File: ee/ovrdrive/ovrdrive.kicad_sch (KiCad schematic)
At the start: 41 parts, among them J1 USB_A, J3 AVR-ISP-6, U1 SM3257ENT, U2 FLASH, U3 ATtiny24A-MM, U4 SN74LVC1G32DCKR, U5 DRV8837C

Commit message: R0.3 released
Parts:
- added C15, C16: 100nF, Capacitor_SMD:C_0603_1608Metric, symbol Device:C_Small
- R14, R15: footprint Resistor_SMD:R_0402_1005Metric -> Resistor_SMD:R_0603_1608Metric
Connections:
- net +3.3V: now also C15.1
- net +5V: now also C16.1
- net GND: now also C15.2, C16.2
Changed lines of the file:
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@@
   (junction (at 71.12 62.865) (diameter 0) (color 0 0 0 0)
   )
+  (junction (at 196.85 109.855) (diameter 0) (color 0 0 0 0)
+  )
   (junction (at 54.61 176.53) (diameter 0) (color 0 0 0 0)
   )
@@
   (junction (at 104.14 46.99) (diameter 0) (color 0 0 0 0)
   )
+  (junction (at 189.23 109.855) (diameter 0) (color 0 0 0 0)
+  )
   (junction (at 177.8 116.84) (diameter 0) (color 0 0 0 0)
   )
@@
     (stroke (width 0) (type default))
   )
+  (wire (pts (xy 189.23 109.855) (xy 189.23 110.49))
+    (stroke (width 0) (type default))
+  )
   (wire (pts (xy 104.775 89.535) (xy 99.06 89.535))
     (stroke (width 0) (type default))
@@
     (stroke (width 0) (type default))
   )
+  (wire (pts (xy 191.77 109.855) (xy 191.77 118.11))
+    (stroke (width 0) (type default))
+  )
   (wire (pts (xy 76.835 62.865) (xy 76.835 64.77))
     (stroke (width 0) (type default))
@@
     (stroke (width 0) (type default))
   )
+  (wire (pts (xy 196.85 109.855) (xy 196.85 110.49))
+    (stroke (width 0) (type default))
+  )
   (wire (pts (xy 37.465 59.055) (xy 43.18 59.055))
     (stroke (width 0) (type default))
@@
     (stroke (width 0) (type default))
   )
+  (wire (pts (xy 189.23 115.57) (xy 189.23 116.205))
+    (stroke (width 0) (type default))
+  )
   (wire (pts (xy 153.67 74.93) (xy 153.67 76.2))
     (stroke (width 0) (type default))
@@
     (stroke (width 0) (type default))
   )
-  (wire (pts (xy 191.77 109.855) (xy 191.77 118.11))
+  (wire (pts (xy 189.23 104.775) (xy 189.23 109.855))
     (stroke (width 0) (type default))
   )
@@
     (stroke (width 0) (type default))
   )
+  (wire (pts (xy 189.23 109.855) (xy 191.77 109.855))
+    (stroke (width 0) (type default))
+  )
   (wire (pts (xy 204.47 138.43) (xy 205.74 138.43))
     (stroke (width 0) (type default))
@@
     (stroke (width 0) (type default))
   )
-  (wire (pts (xy 194.31 114.935) (xy 194.31 118.11))
+  (wire (pts (xy 196.85 104.775) (xy 196.85 109.855))
     (stroke (width 0) (type default))
   )
@@
     (stroke (width 0) (type default))
   )
+  (wire (pts (xy 196.85 115.57) (xy 196.85 116.205))
+    (stroke (width 0) (type default))
+  )
   (wire (pts (xy 80.645 64.77) (xy 80.645 62.865))
     (stroke (width 0) (type default))
@@
     (stroke (width 0) (type default))
   )
+  (wire (pts (xy 194.31 109.855) (xy 194.31 118.11))
+    (stroke (width 0) (type default))
+  )
   (wire (pts (xy 170.18 87.63) (xy 173.355 87.63))
     (stroke (width 0) (type default))
@@
   )
   (wire (pts (xy 184.15 130.81) (xy 173.99 130.81))
+    (stroke (width 0) (type default))
+  )
+  (wire (pts (xy 196.85 109.855) (xy 194.31 109.855))
     (stroke (width 0) (type default))
   )
@@
         (path "/73c7e5ea-07c9-44ef-a9f8-630a9b8be271"
           (reference "#PWR036") (unit 1)
+        )
+      )
+    )
+  )
+  (symbol (lib_id "Device:C_Small") (at 196.85 113.03 0) (unit 1)
+    (in_bom yes) (on_board yes) (dnp no)
+    (property "Reference" "C15" (at 198.12 109.22 0)
+      (effects (font (size 1.27 1.27)) (justify left))
+    )
+    (property "Value" "100nF" (at 198.12 111.125 0)
+      (effects (font (size 1.27 1.27)) (justify left))
+    )
+    (property "Footprint" "Capacitor_SMD:C_0603_1608Metric" (at 196.85 113.03 0)
+      (effects (font (size 1.27 1.27)) hide)
+    )
+    (property "Datasheet" "~" (at 196.85 113.03 0)
+      (effects (font (size 1.27 1.27)) hide)
+    )
+    (property "MPN" "CC0603KRX7R7BB104" (at 196.85 113.03 0)
+      (effects (font (size 1.27 1.27)) hide)
+    )
+    (pin "1")
+    (pin "2")
+    (instances
+      (project "ovrdrive"
+        (path "/73c7e5ea-07c9-44ef-a9f8-630a9b8be271"
+          (reference "C15") (unit 1)
         )
       )
@@
       (effects (font (size 1.27 1.27)) (justify right))
     )
-    (property "Footprint" "Resistor_SMD:R_0402_1005Metric" (at 173.99 138.43 0)
+    (property "Footprint" "Resistor_SMD:R_0603_1608Metric" (at 173.99 138.43 0)
       (effects (font (size 1.27 1.27)) hide)
     )
@@
     )
   )
+  (symbol (lib_id "Device:C_Small") (at 189.23 113.03 0) (mirror y) (unit 1)
+    (in_bom yes) (on_board yes) (dnp no)
+    (property "Reference" "C16" (at 187.96 109.22 0)
+      (effects (font (size 1.27 1.27)) (justify left))
+    )
+    (property "Value" "100nF" (at 187.96 111.125 0)
+      (effects (font (size 1.27 1.27)) (justify left))
+    )
+    (property "Footprint" "Capacitor_SMD:C_0603_1608Metric" (at 189.23 113.03 0)
+      (effects (font (size 1.27 1.27)) hide)
+    )
+    (property "Datasheet" "~" (at 189.23 113.03 0)
+      (effects (font (size 1.27 1.27)) hide)
+    )
+    (property "MPN" "CC0603KRX7R7BB104" (at 189.23 113.03 0)
+      (effects (font (size 1.27 1.27)) hide)
+    )
+    (pin "1")
+    (pin "2")
+    (instances
+      (project "ovrdrive"
+        (path "/73c7e5ea-07c9-44ef-a9f8-630a9b8be271"
+          (reference "C16") (unit 1)
+        )
+      )
+    )
+  )
   (symbol (lib_id "power:GND") (at 20.32 76.2 0) (unit 1)
     (in_bom yes) (on_board yes) (dnp no)
@@
     )
   )
-  (symbol (lib_id "power:+5V") (at 191.77 109.855 0) (unit 1)
-    (in_bom yes) (on_board yes) (dnp no) (fields_autoplaced)
-    (property "Reference" "#PWR038" (at 191.77 113.665 0)
-      (effects (font (size 1.27 1.27)) hide)
-    )
-    (property "Value" "+5V" (at 191.77 106.2792 0)
-      (effects (font (size 1.27 1.27)))
-    )
-    (property "Footprint" "" (at 191.77 109.855 0)
-      (effects (font (size 1.27 1.27)) hide)
-    )
-    (property "Datasheet" "" (at 191.77 109.855 0)
+  (symbol (lib_id "power:+5V") (at 189.23 104.775 0) (unit 1)
+    (in_bom yes) (on_board yes) (dnp no) (fields_autoplaced)
+    (property "Reference" "#PWR038" (at 189.23 108.585 0)
+      (effects (font (size 1.27 1.27)) hide)
+    )
+    (property "Value" "+5V" (at 189.23 101.1992 0)
+      (effects (font (size 1.27 1.27)))
+    )
+    (property "Footprint" "" (at 189.23 104.775 0)
+      (effects (font (size 1.27 1.27)) hide)
+    )
+    (property "Datasheet" "" (at 189.23 104.775 0)
       (effects (font (size 1.27 1.27)) hide)
     )
@@
     )
   )
+  (symbol (lib_id "power:GND") (at 196.85 116.205 0) (unit 1)
+    (in_bom yes) (on_board yes) (dnp no) (fields_autoplaced)
+    (property "Reference" "#PWR07" (at 196.85 122.555 0)
+      (effects (font (size 1.27 1.27)) hide)
+    )
+    (property "Value" "GND" (at 196.85 120.6484 0)
+      (effects (font (size 1.27 1.27)) hide)
+    )
+    (property "Footprint" "" (at 196.85 116.205 0)
+      (effects (font (size 1.27 1.27)) hide)
+    )
+    (property "Datasheet" "" (at 196.85 116.205 0)
+      (effects (font (size 1.27 1.27)) hide)
+    )
+    (pin "1")
+    (instances
+      (project "ovrdrive"
+        (path "/73c7e5ea-07c9-44ef-a9f8-630a9b8be271"
+          (reference "#PWR07") (unit 1)
+        )
+      )
+    )
+  )
   (symbol (lib_id "Device:R_Small_US") (at 173.99 123.825 0) (mirror x) (unit 1)
     (in_bom yes) (on_board yes) (dnp no)
@@
       (effects (font (size 1.27 1.27)) (justify right))
     )
-    (property "Footprint" "Resistor_SMD:R_0402_1005Metric" (at 173.99 123.825 0)
+    (property "Footprint" "Resistor_SMD:R_0603_1608Metric" (at 173.99 123.825 0)
       (effects (font (size 1.27 1.27)) hide)
     )
@@
     )
   )
-  (symbol (lib_id "power:+3.3V") (at 194.31 114.935 0) (unit 1)
-    (in_bom yes) (on_board yes) (dnp no) (fields_autoplaced)
-    (property "Reference" "#PWR037" (at 194.31 118.745 0)
-      (effects (font (size 1.27 1.27)) hide)
-    )
-    (property "Value" "+3.3V" (at 194.31 111.3592 0)
-      (effects (font (size 1.27 1.27)))
-    )
-    (property "Footprint" "" (at 194.31 114.935 0)
-      (effects (font (size 1.27 1.27)) hide)
-    )
-    (property "Datasheet" "" (at 194.31 114.935 0)
+  (symbol (lib_id "power:+3.3V") (at 196.85 104.775 0) (unit 1)
+    (in_bom yes) (on_board yes) (dnp no)
+    (property "Reference" "#PWR037" (at 196.85 108.585 0)
+      (effects (font (size 1.27 1.27)) hide)
+    )
+    (property "Value" "+3.3V" (at 196.85 101.1992 0)
+      (effects (font (size 1.27 1.27)))
+    )
+    (property "Footprint" "" (at 196.85 104.775 0)
+      (effects (font (size 1.27 1.27)) hide)
+    )
+    (property "Datasheet" "" (at 196.85 104.775 0)
       (effects (font (size 1.27 1.27)) hide)
     )
@@
         )
       )
+    )
+  )
+  (symbol (lib_id "power:GND") (at 189.23 116.205 0) (mirror y) (unit 1)
+    (in_bom yes) (on_board yes) (dnp no) (fields_autoplaced)
+    (property "Reference" "#PWR011" (at 189.23 122.555 0)
+      (effects (font (size 1.27 1.27)) hide)
+    )
+    (property "Value" "GND" (at 189.23 120.6484 0)
+      (effects (font (size 1.27 1.27)) hide)
+    )
+    (property "Footprint" "" (at 189.23 116.205 0)
+      (effects (font (size 1.27 1.27)) hide)
+    )
+    (property "Datasheet" "" (at 189.23 116.205 0)
+      (effects (font (size 1.27 1.27)) hide)
+    )
+    (pin "1")
+    (instances
+      (project "ovrdrive"
+        (path "/73c7e5ea-07c9-44ef-a9f8-630a9b8be271"
+          (reference "#PWR011") (unit 1)
+        )
+      )

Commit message: Added BOM commmited leftover stuff.
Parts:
- R1, R2: MPN (none) -> RC0402FR-071ML
- U5: MPN (none) -> DRV8837CDSGR
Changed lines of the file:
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@@
       (effects (font (size 1.27 1.27)) hide)
     )
-    (property "MPN" "" (at 62.23 176.53 90)
+    (property "MPN" "RC0402FR-071ML" (at 62.23 176.53 90)
       (effects (font (size 1.27 1.27)) hide)
     )
@@
       (effects (font (size 1.27 1.27)) hide)
     )
-    (property "MPN" "" (at 33.655 176.53 90)
+    (property "MPN" "RC0402FR-071ML" (at 33.655 176.53 90)
       (effects (font (size 1.27 1.27)) hide)
     )
@@
       (effects (font (size 1.27 1.27)) hide)
     )
+    (property "MPN" "DRV8837CDSGR" (at 194.31 130.81 0)
+      (effects (font (size 1.27 1.27)) hide)
+    )

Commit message: Added license
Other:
- moved on the sheet: C15, C16, R14, R15, U5

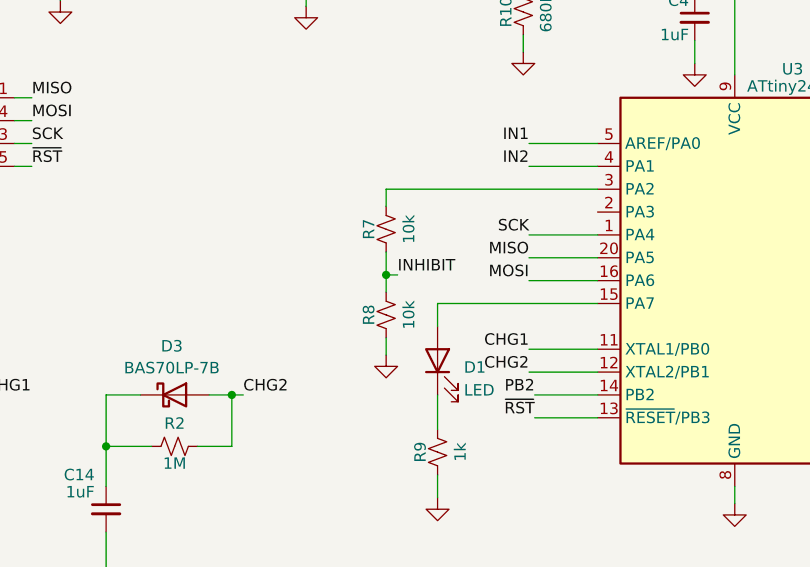
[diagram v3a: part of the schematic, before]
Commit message: Released R0.4 for *quote only*. Still need to do a final revision before sending off.
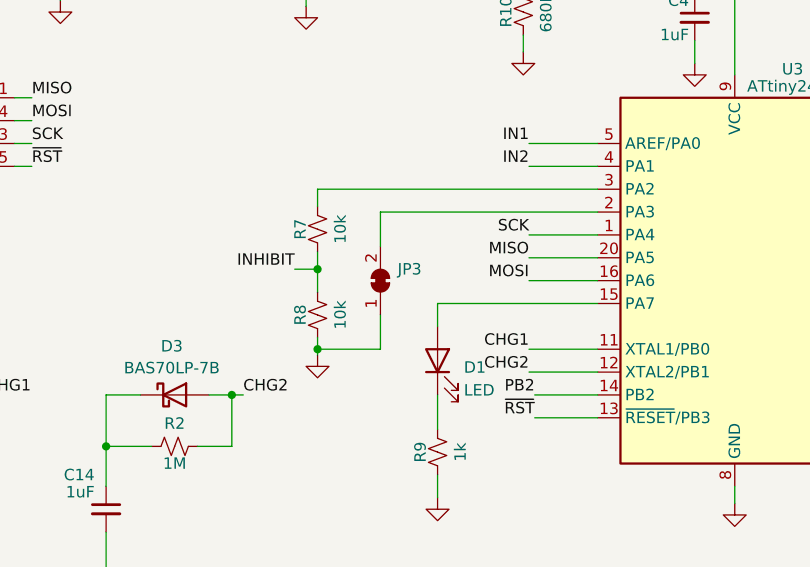
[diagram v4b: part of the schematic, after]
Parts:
- added JP3: SolderJumper_2_Bridged, Jumper:SolderJumper-2_P1.3mm_Bridged2Bar_RoundedPad1.0x1.5mm, symbol Jumper:SolderJumper_2_Bridged
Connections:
- net GND: now also JP3.1 (A)
- net at U3.2 (PA3): now also JP3.2 (B)
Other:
- moved on the sheet: R7, R8
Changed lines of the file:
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@@
   (junction (at 26.035 176.53) (diameter 0) (color 0 0 0 0)
   )
+  (junction (at 78.105 165.735) (diameter 0) (color 0 0 0 0)
+  )
   (junction (at 31.75 88.9) (diameter 0) (color 0 0 0 0)
   )
@@
   (junction (at 82.55 62.865) (diameter 0) (color 0 0 0 0)
   )
-  (junction (at 85.725 157.48) (diameter 0) (color 0 0 0 0)
-  )
   (junction (at 71.12 62.865) (diameter 0) (color 0 0 0 0)
   )
@@
   (junction (at 71.12 46.99) (diameter 0) (color 0 0 0 0)
   )
+  (junction (at 78.105 156.845) (diameter 0) (color 0 0 0 0)
+  )
   (junction (at 76.835 125.095) (diameter 0) (color 0 0 0 0)
   )
@@
     (stroke (width 0) (type default))
   )
+  (wire (pts (xy 85.09 165.735) (xy 78.105 165.735))
+    (stroke (width 0) (type default))
+  )
   (wire (pts (xy 54.61 111.125) (xy 46.99 111.125))
     (stroke (width 0) (type default))
@@
     (stroke (width 0) (type default))
   )
-  (wire (pts (xy 109.22 147.955) (xy 85.725 147.955))
-    (stroke (width 0) (type default))
-  )
   (wire (pts (xy 149.225 76.2) (xy 149.225 77.47))
     (stroke (width 0) (type default))
@@
     (stroke (width 0) (type default))
   )
+  (wire (pts (xy 85.09 150.495) (xy 109.22 150.495))
+    (stroke (width 0) (type default))
+  )
   (wire (pts (xy 120.015 131.445) (xy 120.015 133.985))
     (stroke (width 0) (type default))
@@
     (stroke (width 0) (type default))
   )
+  (wire (pts (xy 75.565 156.845) (xy 78.105 156.845))
+    (stroke (width 0) (type default))
+  )
   (wire (pts (xy 73.025 122.555) (xy 73.025 125.095))
     (stroke (width 0) (type default))
@@
     (stroke (width 0) (type default))
   )
-  (wire (pts (xy 85.725 157.48) (xy 86.995 157.48))
-    (stroke (width 0) (type default))
-  )
   (wire (pts (xy 139.7 95.25) (xy 99.06 95.25))
     (stroke (width 0) (type default))
@@
     (stroke (width 0) (type default))
   )
-  (wire (pts (xy 85.725 147.955) (xy 85.725 149.86))
+  (wire (pts (xy 78.105 147.955) (xy 78.105 149.86))
     (stroke (width 0) (type default))
   )
@@
     (stroke (width 0) (type default))
   )
+  (wire (pts (xy 78.105 165.735) (xy 78.105 166.37))
+    (stroke (width 0) (type default))
+  )
   (wire (pts (xy 149.225 69.85) (xy 149.225 68.58))
     (stroke (width 0) (type default))
@@
     (stroke (width 0) (type default))
   )
+  (wire (pts (xy 85.09 161.925) (xy 85.09 165.735))
+    (stroke (width 0) (type default))
+  )
   (wire (pts (xy 111.125 39.37) (xy 111.125 40.64))
     (stroke (width 0) (type default))
@@
     (stroke (width 0) (type default))
   )
+  (wire (pts (xy 78.105 156.845) (xy 78.105 159.385))
+    (stroke (width 0) (type default))
+  )
   (wire (pts (xy 143.51 68.58) (xy 149.225 68.58))
     (stroke (width 0) (type default))
@@
     (stroke (width 0) (type default))
   )
-  (wire (pts (xy 85.725 154.94) (xy 85.725 157.48))
-    (stroke (width 0) (type default))
-  )
   (wire (pts (xy 65.405 40.64) (xy 65.405 39.37))
     (stroke (width 0) (type default))
@@
     (stroke (width 0) (type default))
   )
+  (wire (pts (xy 85.09 150.495) (xy 85.09 154.305))
+    (stroke (width 0) (type default))
+  )
   (wire (pts (xy 156.21 114.3) (xy 156.21 116.84))
     (stroke (width 0) (type default))
@@
     (stroke (width 0) (type default))
   )
+  (wire (pts (xy 78.105 147.955) (xy 109.22 147.955))
+    (stroke (width 0) (type default))
+  )
   (wire (pts (xy 80.645 64.77) (xy 80.645 62.865))
     (stroke (width 0) (type default))
@@
     (stroke (width 0) (type default))
   )
-  (wire (pts (xy 85.725 157.48) (xy 85.725 159.385))
+  (wire (pts (xy 78.105 154.94) (xy 78.105 156.845))
     (stroke (width 0) (type default))
   )
@@
     (stroke (width 0) (type default))
   )
-  (wire (pts (xy 85.725 164.465) (xy 85.725 166.37))
+  (wire (pts (xy 78.105 164.465) (xy 78.105 165.735))
     (stroke (width 0) (type default))
   )
@@
     (effects (font (size 1.27 1.27)) (justify left bottom))
   )
-  (label "INHIBIT" (at 86.995 157.48 0) (fields_autoplaced)
-    (effects (font (size 1.27 1.27)) (justify left bottom))
+  (label "INHIBIT" (at 75.565 156.845 180) (fields_autoplaced)
+    (effects (font (size 1.27 1.27)) (justify right bottom))
   )
   (label "~{WP}" (at 52.07 106.045 180) (fields_autoplaced)
@@
     (effects (font (size 1 1)) (justify left bottom))
   )
-  (symbol (lib_id "power:GND") (at 85.725 166.37 0) (unit 1)
+  (symbol (lib_id "power:GND") (at 78.105 166.37 0) (unit 1)
     (in_bom yes) (on_board yes) (dnp no) (fields_autoplaced)
-    (property "Reference" "#PWR028" (at 85.725 172.72 0)
+    (property "Reference" "#PWR028" (at 78.105 172.72 0)
       (effects (font (size 1.27 1.27)) hide)
     )
-    (property "Value" "GND" (at 85.725 170.8134 0)
+    (property "Value" "GND" (at 78.105 170.8134 0)
       (effects (font (size 1.27 1.27)) hide)
     )
-    (property "Footprint" "" (at 85.725 166.37 0)
+    (property "Footprint" "" (at 78.105 166.37 0)
       (effects (font (size 1.27 1.27)) hide)
     )
-    (property "Datasheet" "" (at 85.725 166.37 0)
+    (property "Datasheet" "" (at 78.105 166.37 0)
       (effects (font (size 1.27 1.27)) hide)
     )
@@
     )
   )
-  (symbol (lib_id "Device:R_Small_US") (at 85.725 152.4 180) (unit 1)
+  (symbol (lib_id "Device:R_Small_US") (at 78.105 152.4 180) (unit 1)
     (in_bom yes) (on_board yes) (dnp no)
-    (property "Reference" "R7" (at 83.82 152.4 90)
+    (property "Reference" "R7" (at 76.2 152.4 90)
       (effects (font (size 1.27 1.27)))
     )
-    (property "Value" "10k" (at 88.265 152.4 90)
+    (property "Value" "10k" (at 80.645 152.4 90)
       (effects (font (size 1.27 1.27)))
     )
-    (property "Footprint" "Resistor_SMD:R_0402_1005Metric" (at 85.725 152.4 0)
+    (property "Footprint" "Resistor_SMD:R_0402_1005Metric" (at 78.105 152.4 0)
       (effects (font (size 1.27 1.27)) hide)
     )
-    (property "Datasheet" "~" (at 85.725 152.4 0)
+    (property "Datasheet" "~" (at 78.105 152.4 0)
       (effects (font (size 1.27 1.27)) hide)
     )
-    (property "MPN" "RC0402FR-0710KL" (at 85.725 152.4 90)
+    (property "MPN" "RC0402FR-0710KL" (at 78.105 152.4 90)
       (effects (font (size 1.27 1.27)) hide)
     )
@@
     )
   )
+  (symbol (lib_id "Jumper:SolderJumper_2_Bridged") (at 85.09 158.115 90) (unit 1)
+    (in_bom yes) (on_board yes) (dnp no) (fields_autoplaced)
+    (property "Reference" "JP3" (at 86.995 156.845 90)
+      (effects (font (size 1.27 1.27)) (justify right))
+    )
+    (property "Value" "SolderJumper_2_Bridged" (at 86.995 159.385 90)
+      (effects (font (size 1.27 1.27)) (justify right) hide)
+    )
+    (property "Footprint" "Jumper:SolderJumper-2_P1.3mm_Bridged2Bar_RoundedPad1.0x1.5mm" (at 85.09 158.115 0)
+      (effects (font (size 1.27 1.27)) hide)
+    )
+    (property "Datasheet" "~" (at 85.09 158.115 0)
+      (effects (font (size 1.27 1.27)) hide)
+    )
+    (pin "1")
+    (pin "2")
+    (instances
+      (project "ovrdrive"
+        (path "/73c7e5ea-07c9-44ef-a9f8-630a9b8be271"
+          (reference "JP3") (unit 1)
+        )
+      )
+    )
+  )
   (symbol (lib_id "Driver_Motor:DRV8837C") (at 224.79 138.43 0) (unit 1)
     (in_bom yes) (on_board yes) (dnp no)
@@
     )
   )
-  (symbol (lib_id "Device:R_Small_US") (at 85.725 161.925 180) (unit 1)
+  (symbol (lib_id "Device:R_Small_US") (at 78.105 161.925 180) (unit 1)
     (in_bom yes) (on_board yes) (dnp no)
-    (property "Reference" "R8" (at 83.82 161.925 90)
+    (property "Reference" "R8" (at 76.2 161.925 90)
       (effects (font (size 1.27 1.27)))
     )
-    (property "Value" "10k" (at 88.265 161.925 90)
+    (property "Value" "10k" (at 80.645 161.925 90)
       (effects (font (size 1.27 1.27)))
     )
-    (property "Footprint" "Resistor_SMD:R_0402_1005Metric" (at 85.725 161.925 0)
+    (property "Footprint" "Resistor_SMD:R_0402_1005Metric" (at 78.105 161.925 0)
       (effects (font (size 1.27 1.27)) hide)
     )
-    (property "Datasheet" "~" (at 85.725 161.925 0)
+    (property "Datasheet" "~" (at 78.105 161.925 0)
       (effects (font (size 1.27 1.27)) hide)
     )
-    (property "MPN" "RC0402FR-0710KL" (at 85.725 161.925 90)
+    (property "MPN" "RC0402FR-0710KL" (at 78.105 161.925 90)
       (effects (font (size 1.27 1.27)) hide)
     )

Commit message: Added new part numbers
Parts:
- JP3: now left out of the parts list
- U1: MPN SM3257ENT -> SM3257ENAA
- U2: MPN K9HDG08U1A -> MT29F64G08CBABAWP
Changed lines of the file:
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@@
       (effects (font (size 1.27 1.27)) hide)
     )
-    (property "MPN" "SM3257ENT" (at 76.835 93.345 0)
+    (property "MPN" "SM3257ENAA" (at 76.835 93.345 0)
       (effects (font (size 1.27 1.27)) hide)
     )
@@
       (effects (font (size 1.27 1.27)) (justify left bottom) hide)
     )
-    (property "MPN" "K9HDG08U1A" (at 264.16 40.64 0)
+    (property "MPN" "MT29F64G08CBABAWP" (at 264.16 40.64 0)
       (effects (font (size 1.27 1.27)) hide)
     )
@@
   )
   (symbol (lib_id "Jumper:SolderJumper_2_Bridged") (at 85.09 158.115 90) (unit 1)
-    (in_bom yes) (on_board yes) (dnp no) (fields_autoplaced)
+    (in_bom no) (on_board yes) (dnp no) (fields_autoplaced)
     (property "Reference" "JP3" (at 86.995 156.845 90)
       (effects (font (size 1.27 1.27)) (justify right))
@@
       (effects (font (size 1.27 1.27)) (justify left bottom) hide)
     )
-    (property "MPN" "K9HDG08U1A" (at 154.94 95.25 0)
-      (effects (font (size 1.27 1.27)) hide)
-    )
+    (property "MPN" "MT29F64G08CBABAWP" (at 154.94 95.25 0)
+      (effects (font (size 1.27 1.27)) hide)
+    )
